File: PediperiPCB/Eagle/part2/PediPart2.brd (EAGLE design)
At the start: 45.3 x 27 mm, 11 parts

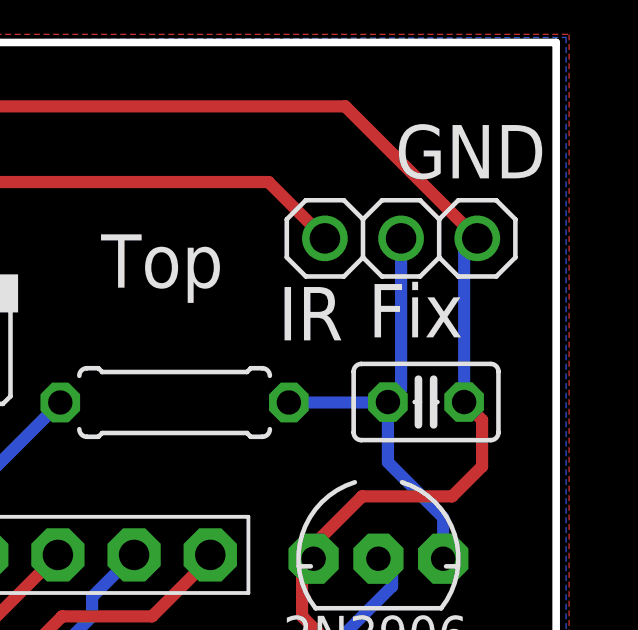
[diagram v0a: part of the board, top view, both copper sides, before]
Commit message: Updated the Resistor values for correction of intensity of LEDS
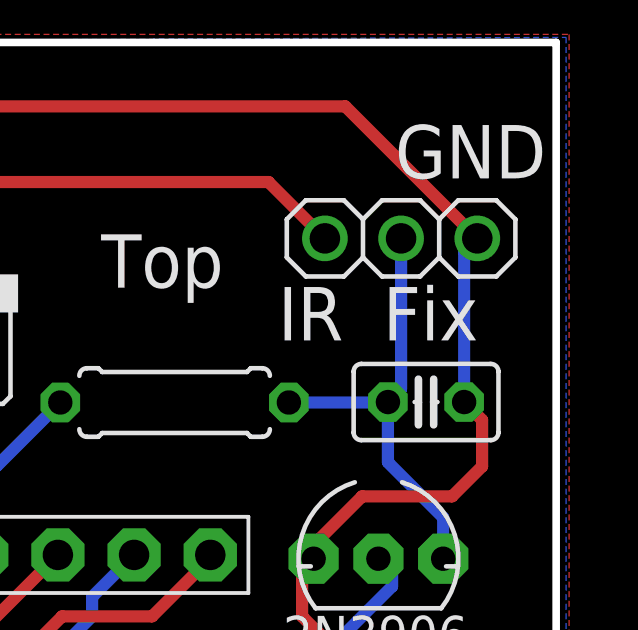
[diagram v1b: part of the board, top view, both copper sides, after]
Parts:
- E$4: value 10K -> 1K2
- E$5: value 10K -> 470E
